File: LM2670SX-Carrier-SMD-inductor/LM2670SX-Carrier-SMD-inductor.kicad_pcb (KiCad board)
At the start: 2 copper layers, 19.6 x 32.4 mm, 10 parts, among them IC1 LM2670SX-3.3_NOPB, J1 Conn_01x03

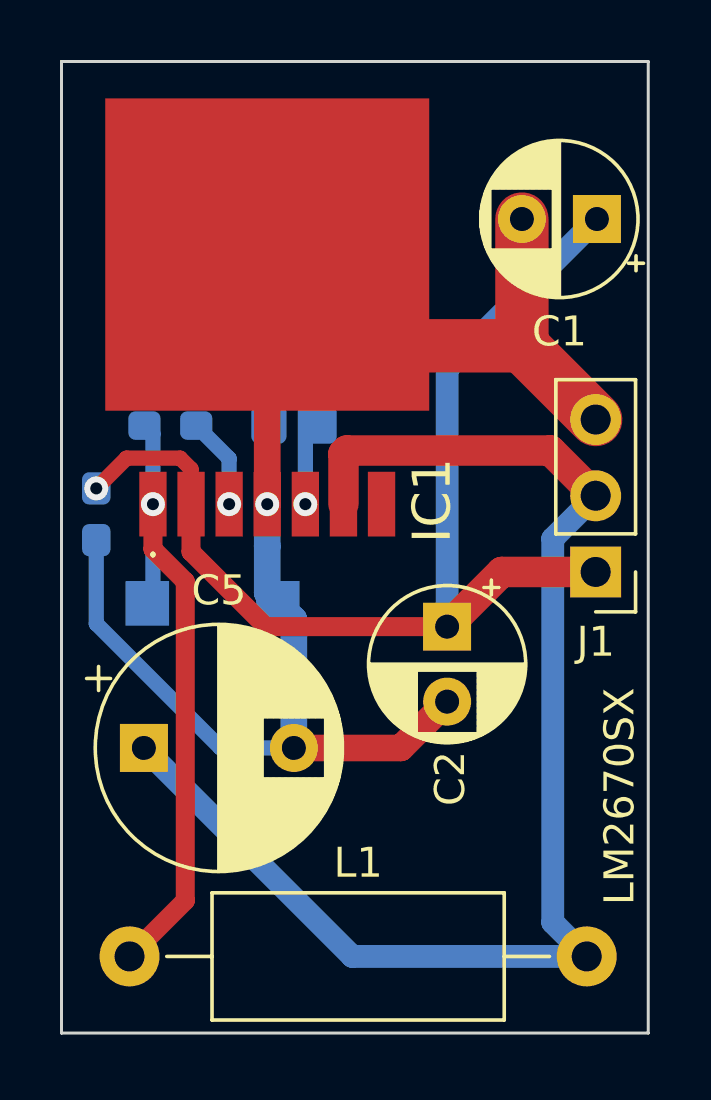
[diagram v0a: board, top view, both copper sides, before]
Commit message: adding fab files for Fixed SMD inductror adding that as well. sent off to fab
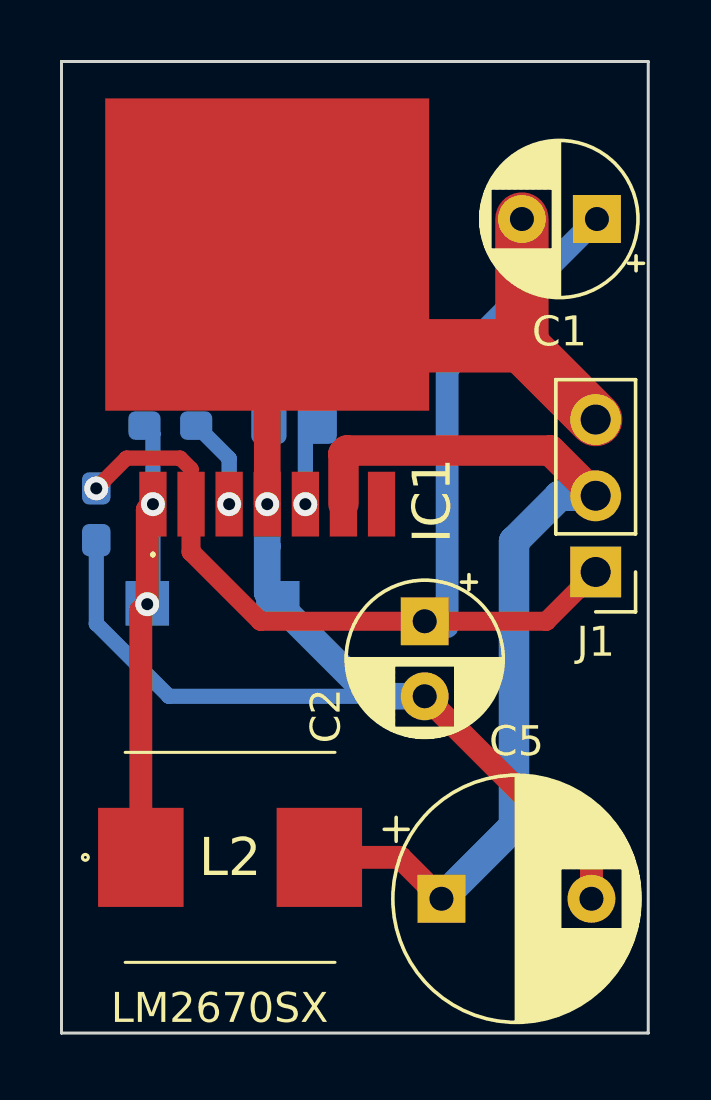
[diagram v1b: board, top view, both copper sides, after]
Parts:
- removed L1: 33mH, Inductor_THT:L_Axial_L9.5mm_D4.0mm_P15.24mm_Horizontal_Fastron_SMCC
- added L2: SPM7054VT-330M-D, SamacSys_Parts:SPM7054VT, F.Cu at (176.6, 111.0)
- moved C5 11.1 mm to (183.6, 112.4)
- moved C2 0.77 mm to (183.0, 103.1)
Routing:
- net +3V3: track 44.8 -> 31.7 mm
- net GND: track 50.5 -> 57.4 mm
- net Net-(IC1-SWITCH_OUTPUT): track 22.1 -> 17.8 mm, vias 1 -> 2

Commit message: adj smd inductor update
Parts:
- C3, C4: footprint Capacitor_SMD:C_0603_1608Metric_Pad1.08x0.95mm_HandSolder -> Capacitor_SMD:C_1206_3216Metric_Pad1.33x1.80mm_HandSolder
- R1: footprint Resistor_SMD:R_0612_1632Metric_Pad1.18x3.40mm_HandSolder -> Capacitor_SMD:C_1206_3216Metric_Pad1.33x1.80mm_HandSolder
- moved C4 6.41 mm to (173.8, 105.7)
- moved C3 3.82 mm to (175.0, 92.8)
- moved R1 3.12 mm to (180.2, 92.8)
- moved D2 2.70 mm to (178.5, 103.3)
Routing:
- net GND: track 57.4 -> 48.3 mm, vias 1 -> 2
- net +VDC: track 37.3 -> 45.4 mm
- net Net-(IC1-SYNC): track 3.90 -> 7.56 mm
- net Net-(IC1-CBOOST/CB): track 3.07 -> 6.42 mm
- net Net-(IC1-SWITCH_OUTPUT): track 17.8 -> 20.6 mm
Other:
- board text added: "GND"
- board text added: "VDC"
- board text added: "VO"
